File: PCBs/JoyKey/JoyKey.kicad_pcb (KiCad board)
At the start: 2 copper layers, 90.2 x 55 mm, 54 parts, among them J1 OLED_DISPLAY, J2 Conn_01x03_Socket, J3 Testpad wire hole1, J4 JST PH, J5 Top Trigger 1, J6 Top Trigger 2, Q1 PMOS,Si7157DP, SW1 RotaryEncoder_Switch, SW2 SW_Push_45deg, SW3 SW_Push_45deg, SW4 SW_Push_45deg, SW5 SW_Push_45deg, SW6 SW_Push_45deg, SW7 SW_Push_45deg, U1 BQ25060, U3 XIAO-RP2040-DIP, U4 LP2981-3.3, U5 2_axis_analog_joystick_button

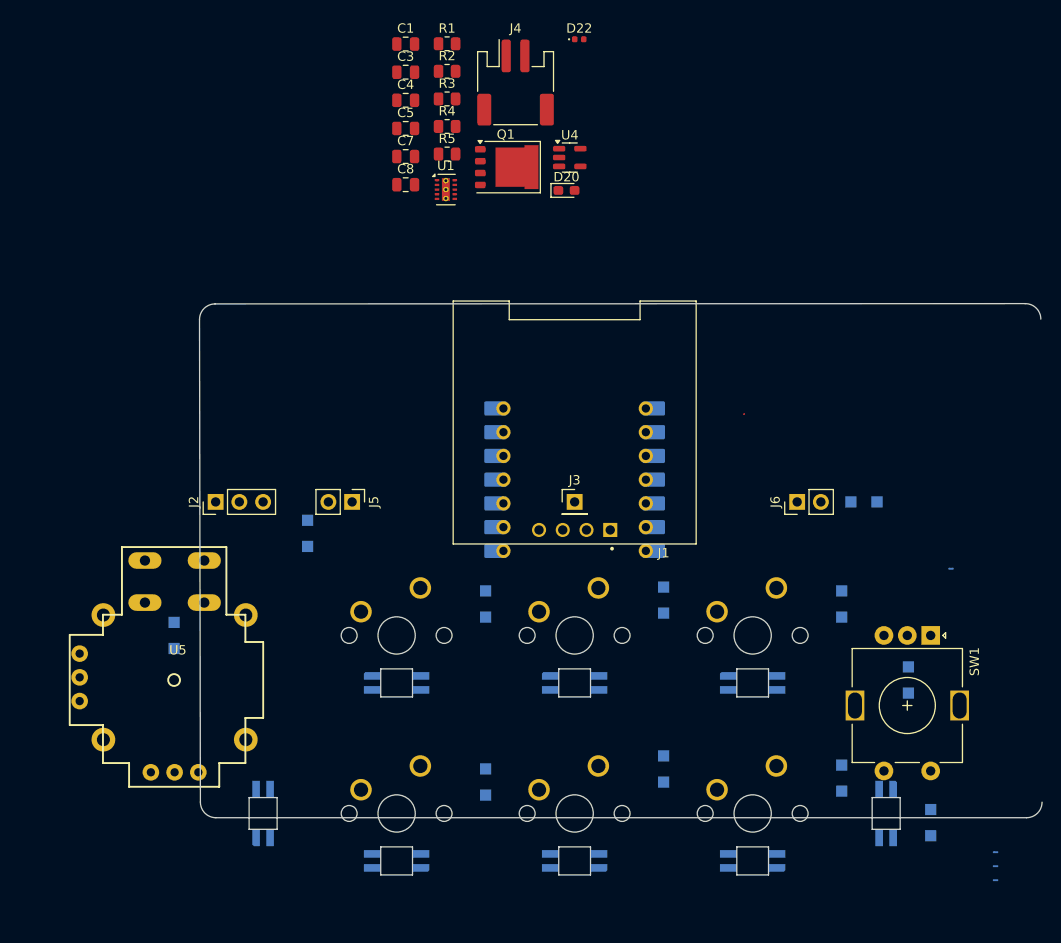
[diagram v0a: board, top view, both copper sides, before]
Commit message: Adjusted Edge Cuts shape
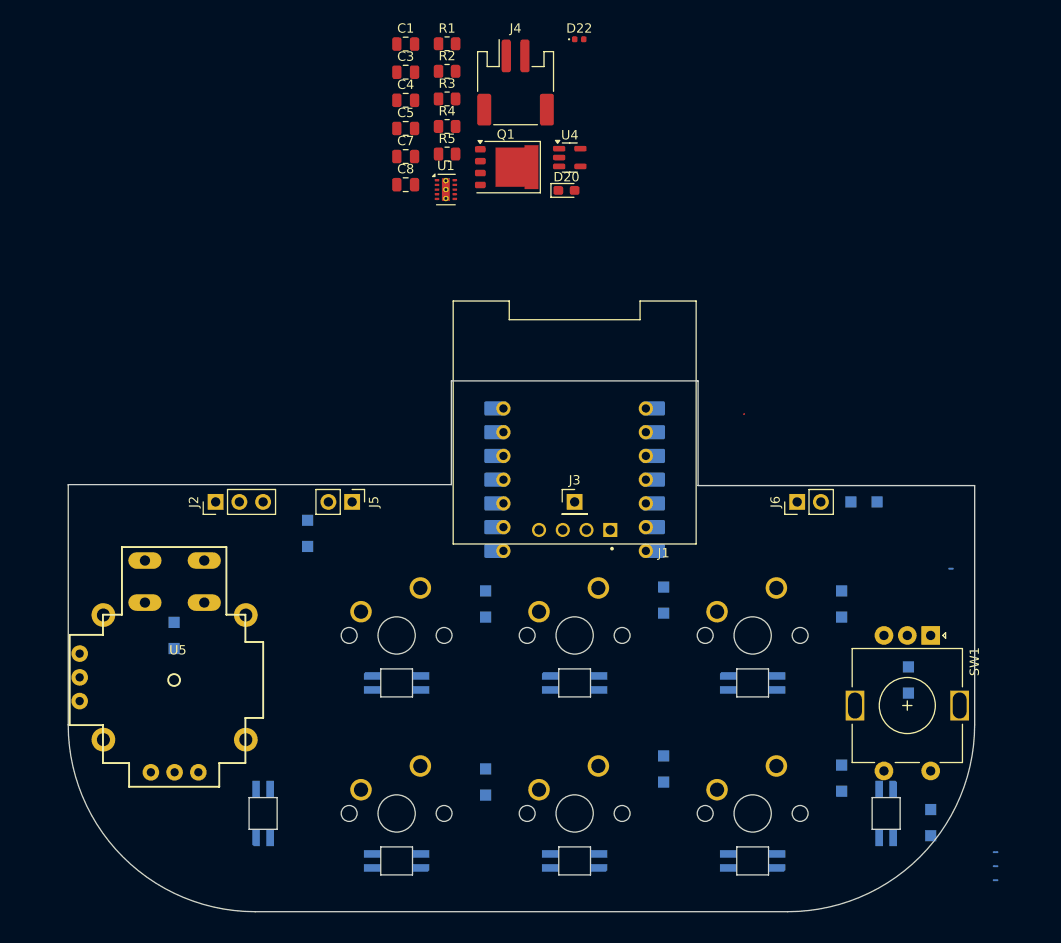
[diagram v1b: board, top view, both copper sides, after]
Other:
- board size 90.2 x 55 mm -> 97 x 56.8 mm
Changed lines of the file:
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@@
 		)
 	)
-	(gr_arc
-		(start 100.350868 75.72504)
-		(mid 100.838 74.549)
-		(end 102.01404 74.061868)
+	(gr_line
+		(start 163.3 139.1)
+		(end 106.3 139.1)
 		(stroke
 			(width 0.05)
@@
 	)
 	(gr_line
-		(start 102.108001 129.044175)
-		(end 188.849003 129.044175)
+		(start 86.3 93.4)
+		(end 86.3 119.1)
 		(stroke
 			(width 0.05)
@@
 	)
 	(gr_line
-		(start 188.722003 74.028829)
-		(end 102.01404 74.061868)
+		(start 183.3 93.5)
+		(end 183.3 119.1)
+		(stroke
+			(width 0.05)
+			(type default)
+		)
+		(layer "Edge.Cuts")
+	)
+	(gr_line
+		(start 153.7 93.5)
+		(end 183.3 93.5)
 		(stroke
 			(width 0.05)
@@
 	)
 	(gr_arc
-		(start 188.722003 74.028829)
-		(mid 189.898043 74.515961)
-		(end 190.385175 75.692001)
+		(start 183.3 119.1)
+		(mid 177.442136 133.242136)
+		(end 163.3 139.1)
 		(stroke
 			(width 0.05)
@@
 	)
 	(gr_line
-		(start 100.350868 75.72504)
-		(end 100.444829 127.381003)
+		(start 86.3 93.4)
+		(end 127.3 93.4)
+		(stroke
+			(width 0.05)
+			(type default)
+		)
+		(layer "Edge.Cuts")
+	)
+	(gr_line
+		(start 127.3 82.3)
+		(end 153.7 82.3)
+		(stroke
+			(width 0.05)
+			(type default)
+		)
+		(layer "Edge.Cuts")
+	)
+	(gr_line
+		(start 153.7 82.3)
+		(end 153.7 93.5)
 		(stroke
 			(width 0.05)
@@
 	)
 	(gr_arc
-		(start 102.108001 129.044175)
-		(mid 100.931961 128.557043)
-		(end 100.444829 127.381003)
+		(start 106.3 139.1)
+		(mid 92.157864 133.242136)
+		(end 86.3 119.1)
 		(stroke
 			(width 0.05)
@@
 		(layer "Edge.Cuts")
 	)
-	(gr_arc
-		(start 190.512175 127.381003)
-		(mid 190.025043 128.557043)
-		(end 188.849003 129.044175)
+	(gr_line
+		(start 127.3 93.4)
+		(end 127.3 82.3)
 		(stroke
 			(width 0.05)

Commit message: Finished Column routing and LED Data routing
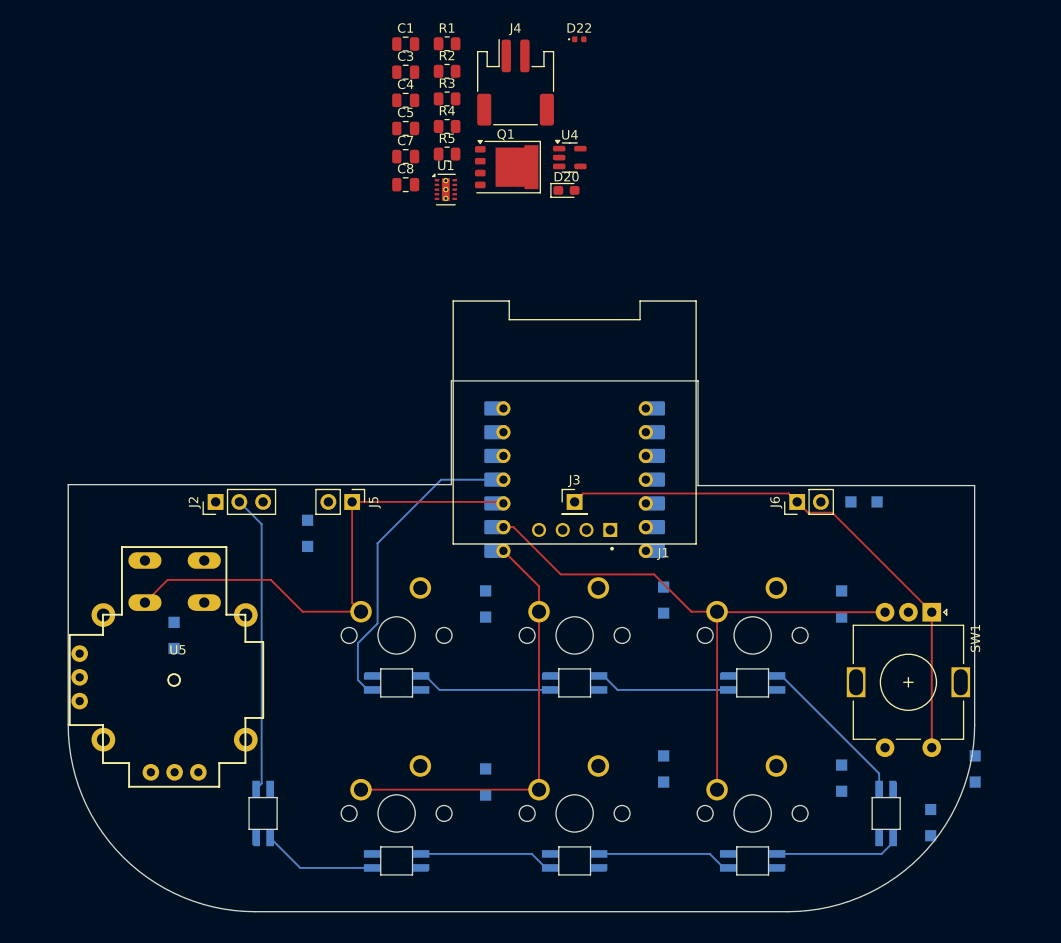
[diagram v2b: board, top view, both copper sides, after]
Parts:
- removed NT1, NT2, NT3, NT4: NetTie_2, custom_Connector:NetTie-2_SMD_Pad0.2mm
- moved D12 11.9 mm to (183.4, 123.8)
- moved SW1 2.49 mm to (178.7, 107.0)
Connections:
- SW1 pad A: /Analog Input/EC11A -> /COL3
- SW1 pad B: /Analog Input/EC11B -> /COL2
- SW1 pad S2: /Analog Input/EC11SWA -> /COL3
- U3 pad 8: /COL2 -> /COL1
- U3 pad 9: /COL1 -> /COL2
- U5 pad B2A: /Analog Input/StickButtonA -> /COL0
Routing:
- net /COL2: track 0.00 -> 63.7 mm
- net /COL3: track 0.00 -> 58.4 mm
- net /COL0: track 0.00 -> 53.9 mm
- net /COL1: track 0.00 -> 46.2 mm
- net /WS2812B: track 0.00 -> 32.9 mm
- net Net-(D19-DOUT): track 0.00 -> 32.0 mm
- net Net-(D6-DOUT): track 0.00 -> 16.9 mm
- net Net-(D21-DOUT): track 0.00 -> 14.5 mm
- net Net-(D10-DOUT): track 0.00 -> 14.5 mm
- net Net-(D5-DOUT): track 0.00 -> 14.5 mm
- net Net-(D10-DIN): track 0.00 -> 14.5 mm
- net Net-(D7-DOUT): track 0.00 -> 13.4 mm
- net Net-(D18-DOUT): track 0.00 -> 12.3 mm

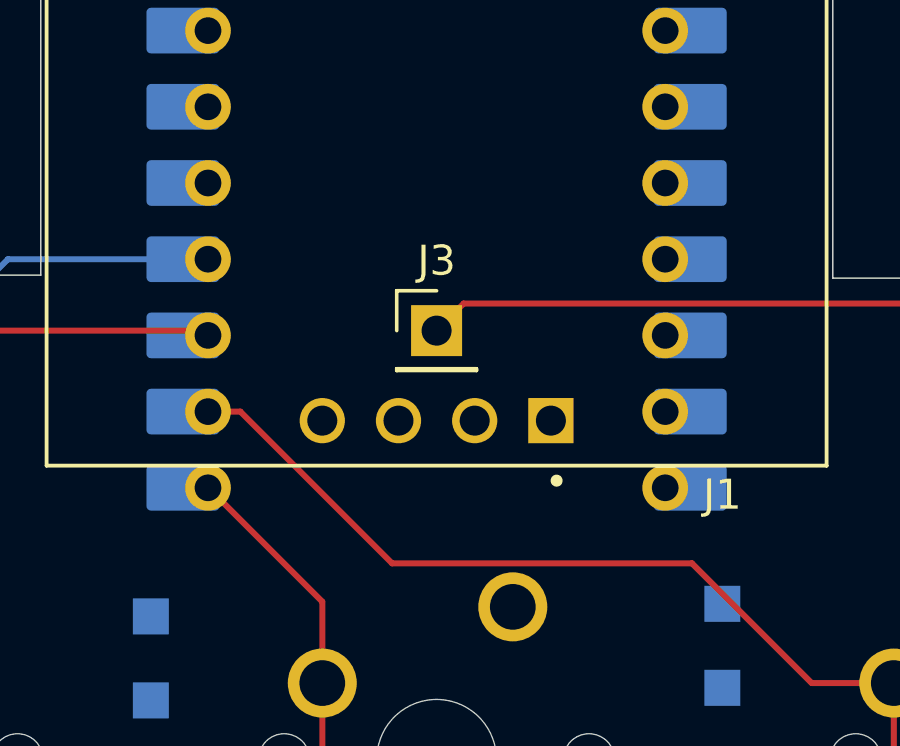
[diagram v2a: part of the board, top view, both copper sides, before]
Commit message: Finished Display Routing
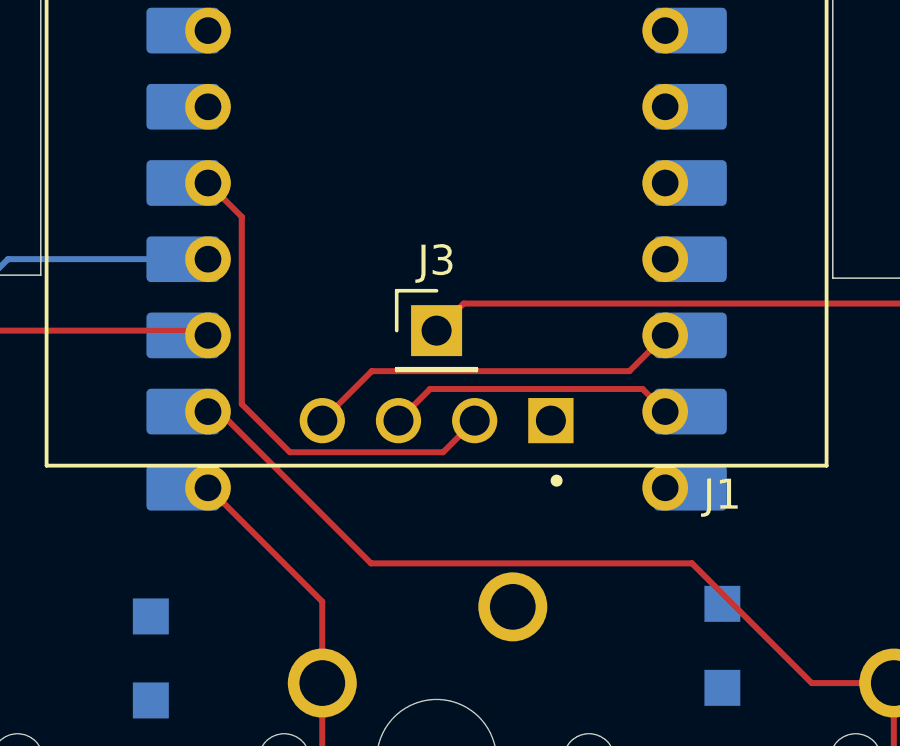
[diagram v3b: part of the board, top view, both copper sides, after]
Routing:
- net +3V3: track 0.00 -> 16.7 mm
- net SDA: track 0.00 -> 12.6 mm
- net SCL: track 0.00 -> 9.64 mm
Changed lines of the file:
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@@
+	)
+	(segment
+		(start 140.70975 99.304)
+		(end 135.604 99.304)
+		(width 0.2)
+		(layer "F.Cu")
+		(net 5)
+	)
+	(segment
+		(start 141.76375 98.25)
+		(end 140.70975 99.304)
+		(width 0.2)
+		(layer "F.Cu")
+		(net 5)
+	)
+	(segment
+		(start 135.604 99.304)
+		(end 134 97.7)
+		(width 0.2)
+		(layer "F.Cu")
+		(net 5)
+	)
+	(segment
+		(start 134 97.7)
+		(end 134 91.455)
+		(width 0.2)
+		(layer "F.Cu")
+		(net 5)
+	)
+	(segment
+		(start 134 91.455)
+		(end 132.87375 90.32875)
+		(width 0.2)
+		(layer "F.Cu")
+		(net 5)
 	)
 	(segment
@@
 	)
 	(segment
+		(start 138.33375 96.6)
+		(end 136.68375 98.25)
+		(width 0.2)
+		(layer "F.Cu")
+		(net 16)
+	)
+	(segment
+		(start 146.9225 96.6)
+		(end 138.33375 96.6)
+		(width 0.2)
+		(layer "F.Cu")
+		(net 16)
+	)
+	(segment
+		(start 148.11375 95.40875)
+		(end 146.9225 96.6)
+		(width 0.2)
+		(layer "F.Cu")
+		(net 16)
+	)
+	(segment
+		(start 139.22375 98.25)
+		(end 140.27775 97.196)
+		(width 0.2)
+		(layer "F.Cu")
+		(net 17)
+	)
+	(segment
+		(start 140.27775 97.196)
+		(end 147.361 97.196)
+		(width 0.2)
+		(layer "F.Cu")
+		(net 17)
+	)
+	(segment
+		(start 147.361 97.196)
+		(end 148.11375 97.94875)
+		(width 0.2)
+		(layer "F.Cu")
+		(net 17)
+	)
+	(segment
 		(start 143.58375 113.8675)
 		(end 145.08375 115.3675)
@@
 	)
 	(segment
-		(start 139.01013 103.0075)
-		(end 149.0075 103.0075)
-		(width 0.2)
-		(layer "F.Cu")
-		(net 35)
-	)
-	(segment
-		(start 132.87375 97.94875)
-		(end 133.95138 97.94875)
-		(width 0.2)
-		(layer "F.Cu")
-		(net 35)
-	)
-	(segment
-		(start 133.95138 97.94875)
-		(end 139.01013 103.0075)
-		(width 0.2)
-		(layer "F.Cu")
-		(net 35)
-	)
-	(segment
 		(start 155.73375 106.9975)
 		(end 155.73375 126.0475)
@@
 	)
 	(segment
+		(start 138.3075 103.0075)
+		(end 149.0075 103.0075)
+		(width 0.2)
+		(layer "F.Cu")
+		(net 35)
+	)
+	(segment
+		(start 155.78625 107.05)
+		(end 155.73375 106.9975)
+		(width 0.2)
+		(layer "F.Cu")
+		(net 35)
+	)
+	(segment
 		(start 152.9975 106.9975)
 		(end 155.73375 106.9975)
@@
 	)
 	(segment
-		(start 155.78625 107.05)
-		(end 155.73375 106.9975)
+		(start 132.87375 97.94875)
+		(end 133.24875 97.94875)
 		(width 0.2)
 		(layer "F.Cu")
@@
 		(width 0.2)
 		(layer "F.Cu")
+		(net 35)
+	)
+	(segment
+		(start 133.24875 97.94875)
+		(end 138.3075 103.0075)
+		(width 0.2)
+		(layer "F.Cu")

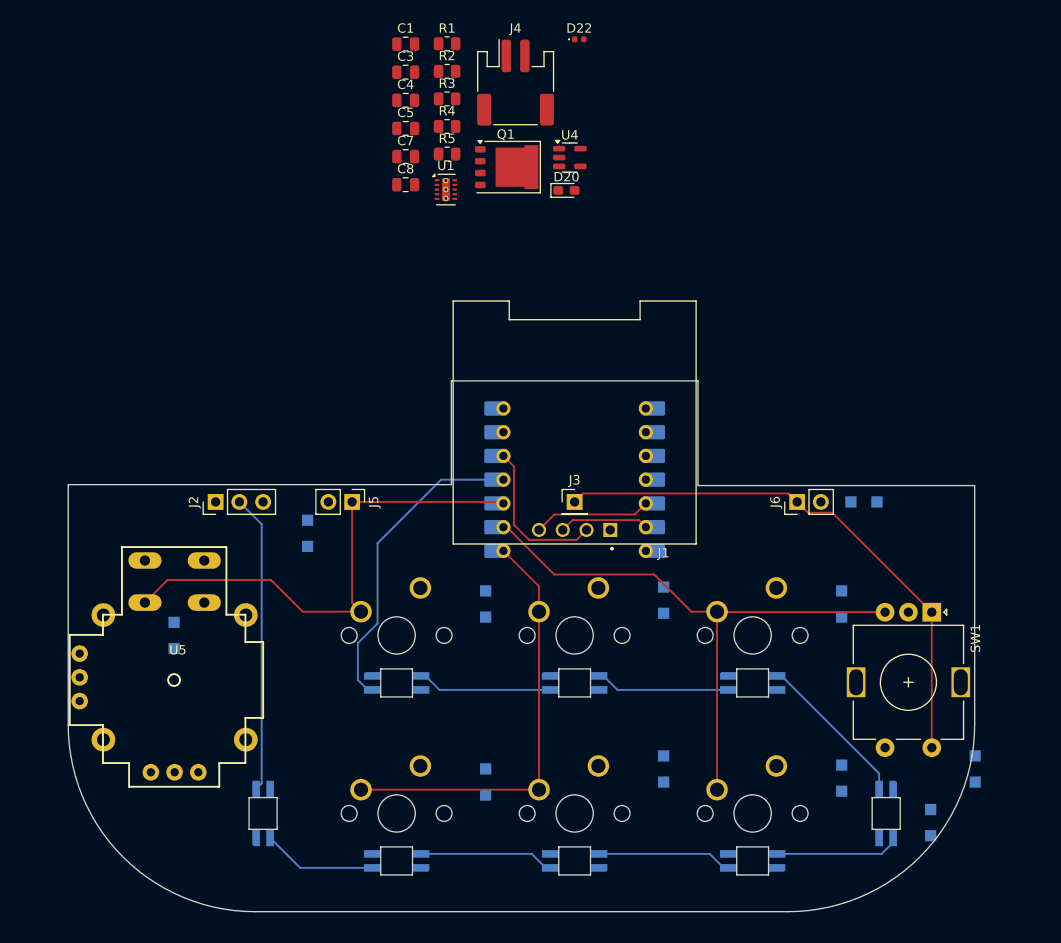
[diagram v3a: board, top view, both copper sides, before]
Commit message: Added Ground Fill
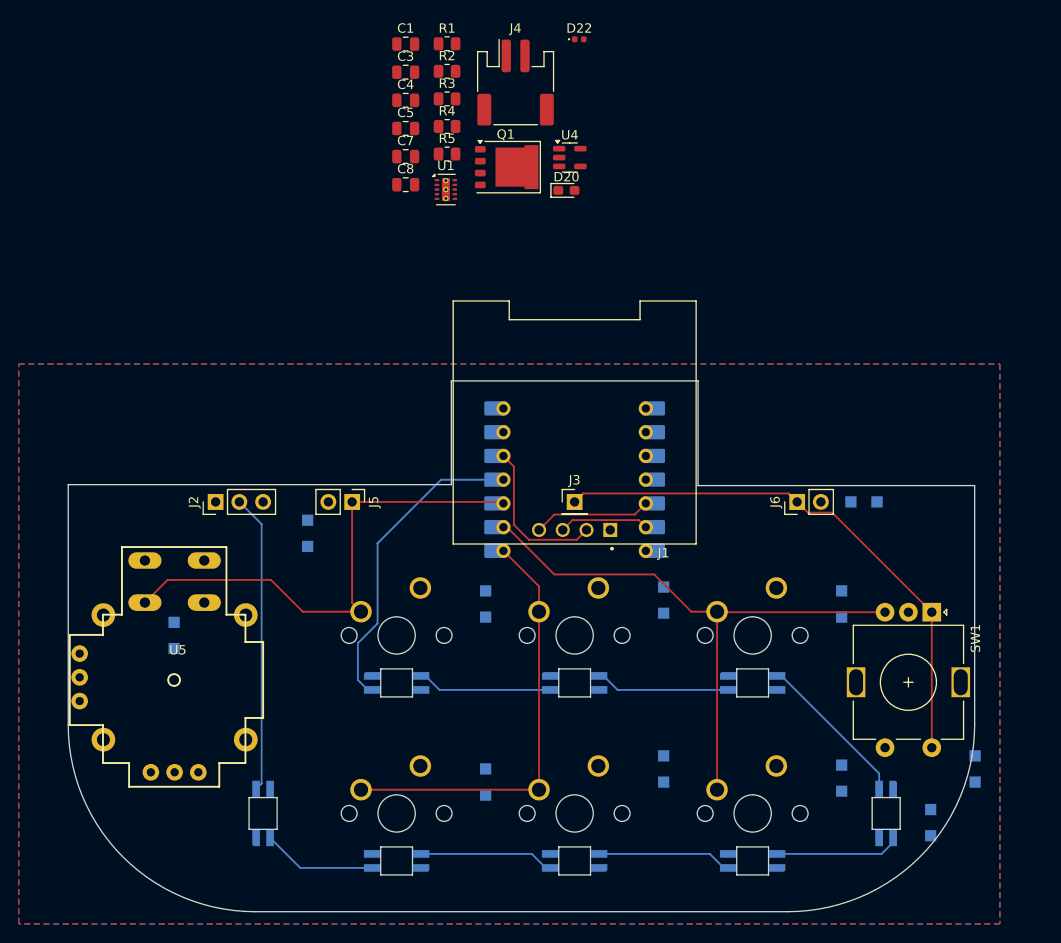
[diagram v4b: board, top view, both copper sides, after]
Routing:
- added copper zone on B.Cu, net GND
- added copper zone on F.Cu, net GND
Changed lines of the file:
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@@
 		(net 38)
 	)
+	(zone
+		(net 7)
+		(net_name "GND")
+		(layers "F&B.Cu")
+		(hatch edge 0.5)
+		(connect_pads
+			(clearance 0.5)
+		)
+		(min_thickness 0.25)
+		(filled_areas_thickness no)
+		(fill yes
+			(thermal_gap 0.5)
+			(thermal_bridge_width 0.5)
+		)
+		(polygon
+			(pts
+				(xy 81 80.5) (xy 186 80.5) (xy 186 140.4) (xy 81 140.4)
+			)
+		)
+	)
 )
